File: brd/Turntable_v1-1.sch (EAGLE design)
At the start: 117 parts, among them CON1 Pannel, CON2 CAN, CON3 Turntable, CON4 STEPPER_CON, CON5 STEPPER_CON, CON8 SPK, IC1 7805, IC2 LM393N, J1 MiniStp2, J10 MiniStp1, Q1 BS170, SW1 EC12E_SW, U2 LED NANO, X1 AK500/2+M, X2 AK500/2+M, X3 MAB 5SH Conrad: 738247 - VQ, X4 AK500/2+M, X5 Reichelt MEBP 8-8S

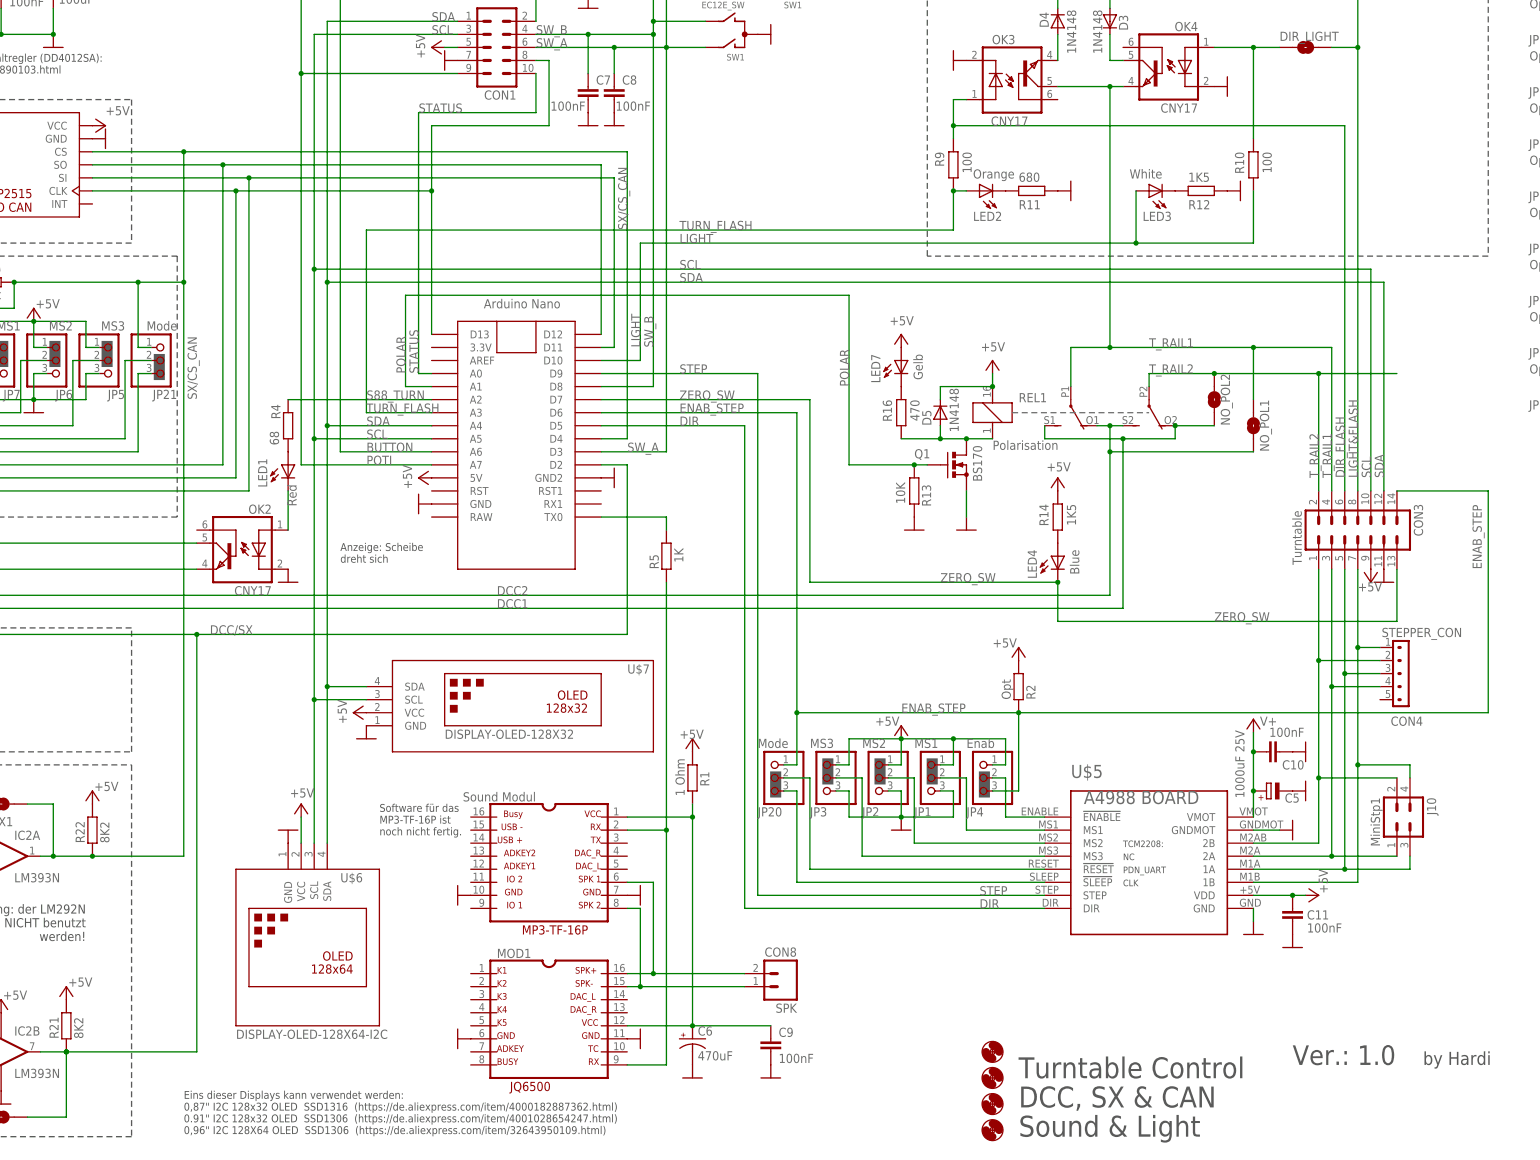
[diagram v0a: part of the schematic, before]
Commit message: Update 2021-04-12
+ R6 and R7, PullUps for I2C
~ CAN-Modul VCC to +5V
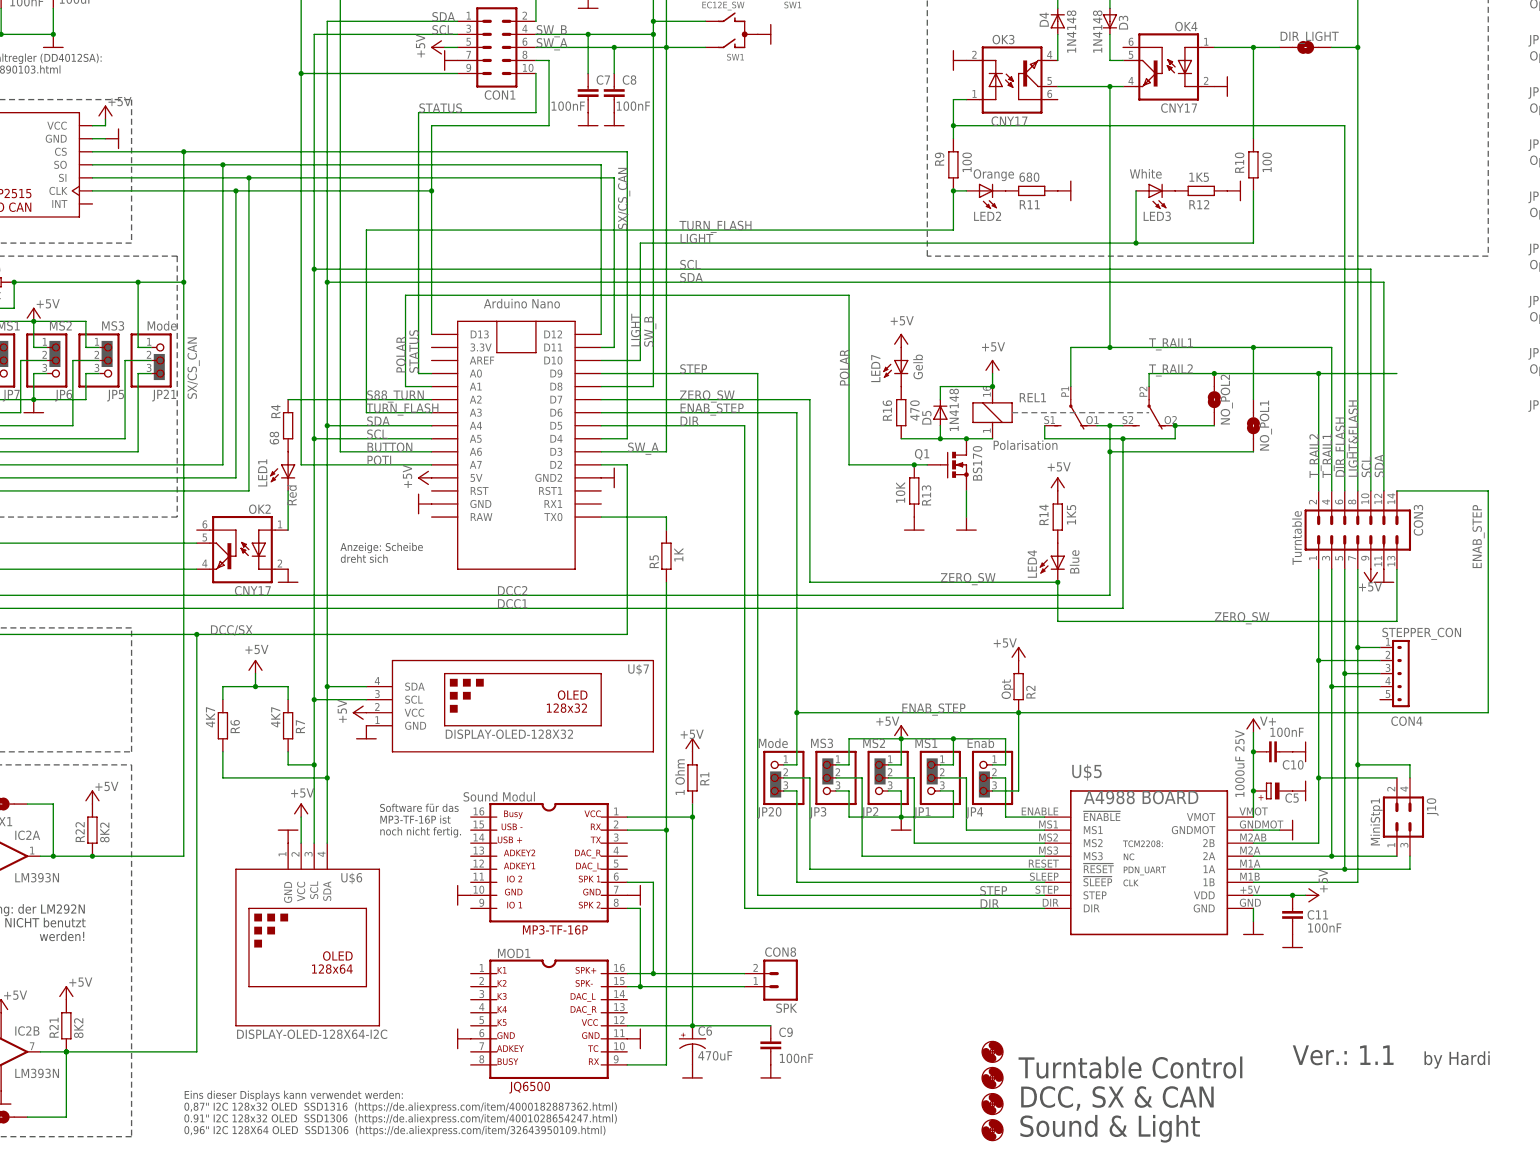
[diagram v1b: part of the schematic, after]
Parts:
- added R6, R7: 4K7, Sound_MP3-TF-16P_and_WS2811:RCL_R-EU_0204/7
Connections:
- removed net VCC: CAN1.VCC
- net +5V: now also CAN1.VCC, R6.1, R7.1
- net SCL: now also R7.2
- net SDA: now also R6.2
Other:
- note added: "Ver.: 1.1"
- note removed: "Ver.: 1.0"
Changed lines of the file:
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@@
 <?xml version="1.0" encoding="utf-8"?>
 <!DOCTYPE eagle SYSTEM "eagle.dtd">
-<eagle version="9.5.2">
+<eagle version="9.6.2">
 <drawing>
 <settings>
-<setting alwaysvectorfont="no"/>
+<setting alwaysvectorfont="yes"/>
 <setting verticaltext="up"/>
 </settings>
-<grid distance="0.1" unitdist="inch" unit="inch" style="lines" multiple="1" display="no" altdistance="0.05" altunitdist="inch" altunit="inch"/>
+<grid distance="0.05" unitdist="inch" unit="inch" style="lines" multiple="1" display="yes" altdistance="0.05" altunitdist="inch" altunit="inch"/>
 <layers>
 <layer number="1" name="Top" color="4" fill="1" visible="no" active="no"/>
@@
 <part name="SJ_SX4" library="SparkFun-Retired" deviceset="SOLDERJUMPER" device="NO"/>
 <part name="GND1" library="supply1" library_urn="urn:adsk.eagle:library:371" deviceset="GND" device=""/>
-<part name="P+1" library="supply1" library_urn="urn:adsk.eagle:library:371" deviceset="+5V" device=""/>
 <part name="GND4" library="supply1" library_urn="urn:adsk.eagle:library:371" deviceset="GND" device=""/>
 <part name="CON2" library="Arduino_fuer_LEDs_DCC_2" deviceset="ML6" device="" value="CAN"/>
@@
 <part name="JP21" library="adafruit" deviceset="PINHD-1X3" device="CB" value="Mode"/>
 <part name="JP8" library="adafruit" deviceset="PINHD-1X3" device="CB" value="Enab"/>
+<part name="R6" library="Sound_MP3-TF-16P_and_WS2811" deviceset="RCL_R-EU_" device="0204/7" value="4K7"/>
+<part name="R7" library="Sound_MP3-TF-16P_and_WS2811" deviceset="RCL_R-EU_" device="0204/7" value="4K7"/>
+<part name="P+27" library="supply1" library_urn="urn:adsk.eagle:library:371" deviceset="+5V" device=""/>
+<part name="P+1" library="supply1" library_urn="urn:adsk.eagle:library:371" deviceset="+5V" device=""/>
 </parts>
 <sheets>
@@
 <text x="379.73" y="205.74" size="1.778" layer="150" rot="R90">House Light</text>
 <text x="368.3" y="20.32" size="2.54" layer="92">by Hardi</text>
-<text x="342.9" y="20.32" size="3.81" layer="97">Ver.: 1.0</text>
+<text x="342.9" y="20.32" size="3.81" layer="97">Ver.: 1.1</text>
 <text x="289.56" y="6.35" size="4.064" layer="97" distance="40">Turntable Control
 DCC, SX &amp; CAN
@@
 <attribute name="NAME" x="31.75" y="39.37" size="1.778" layer="95" rot="MR180"/>
 </instance>
-<instance part="GND1" gate="1" x="111.76" y="200.66" smashed="yes" rot="MR270"/>
-<instance part="P+1" gate="1" x="111.76" y="203.2" smashed="yes" rot="MR90">
-<attribute name="VALUE" x="111.76" y="207.01" size="1.778" layer="96" rot="MR180"/>
-</instance>
+<instance part="GND1" gate="1" x="114.3" y="200.66" smashed="yes" rot="MR270"/>
 <instance part="GND4" gate="1" x="53.34" y="182.88" smashed="yes" rot="MR0"/>
 <instance part="CON2" gate="1" x="55.88" y="195.58" smashed="yes" rot="MR180">
@@
 <attribute name="NAME" x="69.85" y="161.925" size="1.778" layer="95" rot="MR180"/>
 <attribute name="VALUE" x="69.85" y="175.26" size="1.778" layer="96" rot="MR180"/>
+</instance>
+<instance part="R6" gate="G$1" x="134.62" y="86.36" smashed="yes" rot="R270">
+<attribute name="NAME" x="136.1186" y="87.63" size="1.778" layer="95" rot="R270"/>
+<attribute name="VALUE" x="131.318" y="90.17" size="1.778" layer="96" rot="R270"/>
+</instance>
+<instance part="R7" gate="G$1" x="147.32" y="86.36" smashed="yes" rot="R270">
+<attribute name="NAME" x="148.8186" y="87.63" size="1.778" layer="95" rot="R270"/>
+<attribute name="VALUE" x="144.018" y="90.17" size="1.778" layer="96" rot="R270"/>
+</instance>
+<instance part="P+27" gate="1" x="140.97" y="99.06" smashed="yes" rot="MR0">
+<attribute name="VALUE" x="143.51" y="100.33" size="1.778" layer="96" rot="MR0"/>
+</instance>
+<instance part="P+1" gate="1" x="111.76" y="207.01" smashed="yes" rot="MR0">
+<attribute name="VALUE" x="116.84" y="207.01" size="1.778" layer="96" rot="MR0"/>
 </instance>
 </instances>
@@
 <pinref part="GND1" gate="1" pin="GND"/>
 <pinref part="CAN1" gate="1" pin="GND"/>
+<wire x1="111.76" y1="200.66" x2="109.22" y2="200.66" width="0.1524" layer="91"/>
 </segment>
 <segment>
@@
 <pinref part="SV3" gate="G$1" pin="4"/>
 <pinref part="P+26" gate="1" pin="+5V"/>
+</segment>
+<segment>
+<pinref part="P+27" gate="1" pin="+5V"/>
+<wire x1="140.97" y1="96.52" x2="140.97" y2="93.98" width="0.1524" layer="91"/>
+<wire x1="140.97" y1="93.98" x2="134.62" y2="93.98" width="0.1524" layer="91"/>
+<pinref part="R6" gate="G$1" pin="1"/>
+<wire x1="134.62" y1="93.98" x2="134.62" y2="91.44" width="0.1524" layer="91"/>
+<pinref part="R7" gate="G$1" pin="1"/>
+<wire x1="147.32" y1="91.44" x2="147.32" y2="93.98" width="0.1524" layer="91"/>
+<wire x1="147.32" y1="93.98" x2="140.97" y2="93.98" width="0.1524" layer="91"/>
+<junction x="140.97" y="93.98"/>
+</segment>
+<segment>
+<pinref part="CAN1" gate="1" pin="VCC"/>
+<wire x1="109.22" y1="203.2" x2="111.76" y2="203.2" width="0.1524" layer="91"/>
+<pinref part="P+1" gate="1" pin="+5V"/>
+<wire x1="111.76" y1="203.2" x2="111.76" y2="204.47" width="0.1524" layer="91"/>
 </segment>
 </net>
@@
 </segment>
 </net>
-<net name="VCC" class="0">
-<segment>
-<pinref part="P+1" gate="1" pin="+5V"/>
-<pinref part="CAN1" gate="1" pin="VCC"/>
-</segment>
-</net>
 <net name="N$3" class="0">
 <segment>
@@
 <label x="162.56" y="144.78" size="1.778" layer="95"/>
 <pinref part="U$6" gate="G$1" pin="SDA"/>
-<wire x1="154.94" y1="63.5" x2="154.94" y2="93.98" width="0.1524" layer="91"/>
+<wire x1="154.94" y1="63.5" x2="154.94" y2="76.2" width="0.1524" layer="91"/>
 <junction x="154.94" y="144.78"/>
 <pinref part="U$7" gate="G$1" pin="SDA"/>
+<wire x1="154.94" y1="76.2" x2="154.94" y2="93.98" width="0.1524" layer="91"/>
 <wire x1="154.94" y1="93.98" x2="154.94" y2="144.78" width="0.1524" layer="91"/>
 <wire x1="162.56" y1="93.98" x2="154.94" y2="93.98" width="0.1524" layer="91"/>
@@
 <label x="223.52" y="172.72" size="1.778" layer="95"/>
 <pinref part="CON3" gate="1" pin="12"/>
+<pinref part="R6" gate="G$1" pin="2"/>
+<wire x1="134.62" y1="81.28" x2="134.62" y2="76.2" width="0.1524" layer="91"/>
+<wire x1="134.62" y1="76.2" x2="154.94" y2="76.2" width="0.1524" layer="91"/>
+<junction x="154.94" y="76.2"/>
 </segment>
 </net>
@@
 <label x="162.56" y="142.24" size="1.778" layer="95"/>
 <pinref part="U$6" gate="G$1" pin="SCL"/>
-<wire x1="152.4" y1="63.5" x2="152.4" y2="91.44" width="0.1524" layer="91"/>
+<wire x1="152.4" y1="63.5" x2="152.4" y2="78.74" width="0.1524" layer="91"/>
 <junction x="152.4" y="142.24"/>
 <pinref part="U$7" gate="G$1" pin="SCL"/>
+<wire x1="152.4" y1="78.74" x2="152.4" y2="91.44" width="0.1524" layer="91"/>
 <wire x1="152.4" y1="91.44" x2="152.4" y2="142.24" width="0.1524" layer="91"/>
 <wire x1="162.56" y1="91.44" x2="152.4" y2="91.44" width="0.1524" layer="91"/>
 <junction x="152.4" y="91.44"/>
 <label x="223.52" y="175.26" size="1.778" layer="95"/>
-</segment>
-</net>
+<pinref part="R7" gate="G$1" pin="2"/>
+<wire x1="147.32" y1="81.28" x2="147.32" y2="78.74" width="0.1524" layer="91"/>
+<wire x1="147.32" y1="78.74" x2="152.4" y2="78.74" width="0.1524" layer="91"/>
+<junction x="152.4" y="78.74"/>
+</segment>
+</net>
